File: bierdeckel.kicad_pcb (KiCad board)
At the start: 2 copper layers, 93 x 93 mm, 67 parts, among them IC1 HSFPAR004A, J1 Pogo, J2 Pogo, J6 USB4110-GF-A, Q1 BSS138P,215, SW1 PTS526 SK15 SMTR2 LFS, SW2 PTS526 SK15 SMTR2 LFS, SW3 PTS526 SK15 SMTR2 LFS, U1 ESP32-C3-WROOM-02, U2 BQ25176J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

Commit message: replace some components for JLC order
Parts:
- R21: value 4k -> 4k02
- R22: value 4k -> 5k1
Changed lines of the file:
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@@
 			)
 		)
-		(property "mpn" "CR0805-FX-1002ELF "
+		(property "mpn" ""
 			(at 0 0 315)
 			(unlocked yes)
@@
 			)
 		)
-		(property "mpn" "CRCW08054K99FKEA"
+		(property "mpn" ""
 			(at 0 0 180)
 			(unlocked yes)
@@
 			)
 		)
-		(property "mpn" "150060GS73220"
+		(property "mpn" "A-SP192DGHC-C01-4T"
 			(at 0 0 0)
 			(layer "F.Fab")
@@
 		(sheetname "/LEDs/")
 		(sheetfile "leds.kicad_sch")
-		(attr smd)
+		(attr smd exclude_from_bom dnp)
 		(fp_line
 			(start -1 1.05)
@@
 			)
 		)
+		(property "mpn" "ESP32-C3-WROOM-02"
+			(at 0 0 0)
+			(unlocked yes)
+			(layer "F.Fab")
+			(hide yes)
+			(effects
+				(font
+					(size 1 1)
+					(thickness 0.15)
+				)
+			)
+		)
 		(property ki_fp_filters "ESP32?C3*WROOM?02*")
 		(sheetname "/")
@@
 			)
 		)
-		(property "mpn" ""
+		(property "mpn" "BSS138P,215"
 			(at 0 0 180)
 			(unlocked yes)
@@
 			)
 		)
-		(property "mpn" "CRCW080562K0FKEA"
+		(property "mpn" ""
 			(at 0 0 0)
 			(unlocked yes)
@@
 		(sheetfile "bierdeckel.kicad_sch")
 		(zone_connect 1)
-		(attr exclude_from_pos_files allow_soldermask_bridges)
+		(attr exclude_from_pos_files exclude_from_bom dnp allow_soldermask_bridges)
 		(fp_rect
 			(start -0.15 -0.75)
@@
 			)
 		)
+		(property "mpn" "1N4148WT"
+			(at 0 0 0)
+			(unlocked yes)
+			(layer "F.Fab")
+			(hide yes)
+			(effects
+				(font
+					(size 1 1)
+					(thickness 0.15)
+				)
+			)
+		)
 		(property ki_fp_filters "D*SOD?523*")
 		(sheetname "/")
@@
 		(sheetfile "bierdeckel.kicad_sch")
 		(zone_connect 1)
-		(attr exclude_from_pos_files allow_soldermask_bridges)
+		(attr exclude_from_pos_files exclude_from_bom dnp allow_soldermask_bridges)
 		(fp_rect
 			(start -0.15 -0.75)
@@
 			)
 		)
-		(property "mpn" "CRCW08054K99FKEA"
+		(property "mpn" ""
 			(at 0 0 270)
 			(unlocked yes)
@@
 			)
 		)
-		(property "mpn" "CR0805-FX-1002ELF "
+		(property "mpn" ""
 			(at 0 0 90)
 			(unlocked yes)
@@
 			)
 		)
-		(property "mpn" "CRCW080562K0FKEA"
+		(property "mpn" ""
 			(at 0 0 180)
 			(unlocked yes)
@@
 			)
 		)
-		(property "mpn" "CR0805-FX-1002ELF "
+		(property "mpn" ""
 			(at 0 0 90)
 			(unlocked yes)
@@
 			)
 		)
-		(property "mpn" "CR0805-FX-1002ELF "
+		(property "mpn" ""
 			(at 0 0 90)
 			(unlocked yes)
@@
 		(sheetfile "bierdeckel.kicad_sch")
 		(zone_connect 1)
-		(attr exclude_from_pos_files allow_soldermask_bridges)
+		(attr exclude_from_pos_files exclude_from_bom dnp allow_soldermask_bridges)
 		(fp_rect
 			(start -0.15 -0.75)
@@
 			)
 		)
-		(property "mpn" "CR0805-FX-1002ELF "
+		(property "mpn" ""
 			(at 0 0 270)
 			(unlocked yes)
@@
 			)
 		)
-		(property "mpn" "CRCW08054K99FKEA"
+		(property "mpn" ""
 			(at 0 0 270)
 			(unlocked yes)
@@
 			)
 		)
+		(property "mpn" "HSFPAR004A"
+			(at 0 0 315)
+			(unlocked yes)
+			(layer "F.Fab")
+			(hide yes)
+			(effects
+				(font
+					(size 1 1)
+					(thickness 0.15)
+				)
+			)
+		)
 		(sheetname "/Pressure Gauge/")
 		(sheetfile "pressure.kicad_sch")
@@
 			)
 		)
-		(property "mpn" "CRCW080527K4FKEA"
+		(property "mpn" ""
 			(at 0 0 270)
 			(unlocked yes)
@@
 			)
 		)
-		(property "mpn" "CRCW08054K99FKEA"
+		(property "mpn" ""
 			(at 0 0 0)
 			(unlocked yes)
@@
 			)
 		)
-		(property "mpn" "CR0805-FX-6200ELF "
+		(property "mpn" ""
 			(at 0 0 90)
 			(unlocked yes)
@@
 			)
 		)
-		(property "mpn" "CRCW08054K99FKEA"
+		(property "mpn" ""
 			(at 0 0 180)
 			(unlocked yes)
@@
 			)
 		)
-		(property "mpn" "CR0805-FX-1002ELF "
+		(property "mpn" ""
 			(at 0 0 270)
 			(unlocked yes)
@@
 			)
 		)
-		(property "mpn" "CR0805-FX-1002ELF "
+		(property "mpn" ""
 			(at 0 0 180)
 			(unlocked yes)
@@
 			)
 		)
-		(property "mpn" "CR0805-FX-1002ELF "
+		(property "mpn" ""
 			(at 0 0 270)
 			(unlocked yes)
@@
 			)
 		)
-		(property "Value" "4k"
+		(property "Value" "4k02"
 			(at 0 1.83 90)
 			(layer "F.Fab")
@@
 			)
 		)
-		(property "mpn" "CR0805-FX-1002ELF "
+		(property "mpn" "RC1206FR-074K02L"
 			(at 0 0 90)
 			(unlocked yes)
@@
 			)
 		)
-		(property "mpn" "150060BS73220"
+		(property "mpn" "XL-1608UBC-04"
 			(at 0 0 0)
 			(layer "F.Fab")
@@
 			)
 		)
+		(property "mpn" "INA317IDGKR"
+			(at 0 0 270)
+			(unlocked yes)
+			(layer "F.Fab")
+			(hide yes)
+			(effects
+				(font
+					(size 1 1)
+					(thickness 0.15)
+				)
+			)
+		)
 		(sheetname "/Pressure Gauge/")
 		(sheetfile "pressure.kicad_sch")
@@
 			)
 		)
-		(property "mpn" "CL21A106KPFNNNF"
+		(property "mpn" "CL21B105KAFNNNG "
 			(at 0 0 0)
 			(unlocked yes)
@@
 			)
 		)
-		(property "Value" "4k"
+		(property "Value" "5k1"
 			(at 0 1.43 0)
 			(layer "F.Fab")
@@
 			)
 		)
-		(property "mpn" "CR0805-FX-1002ELF "
+		(property "mpn" ""
 			(at 0 0 180)
 			(unlocked yes)

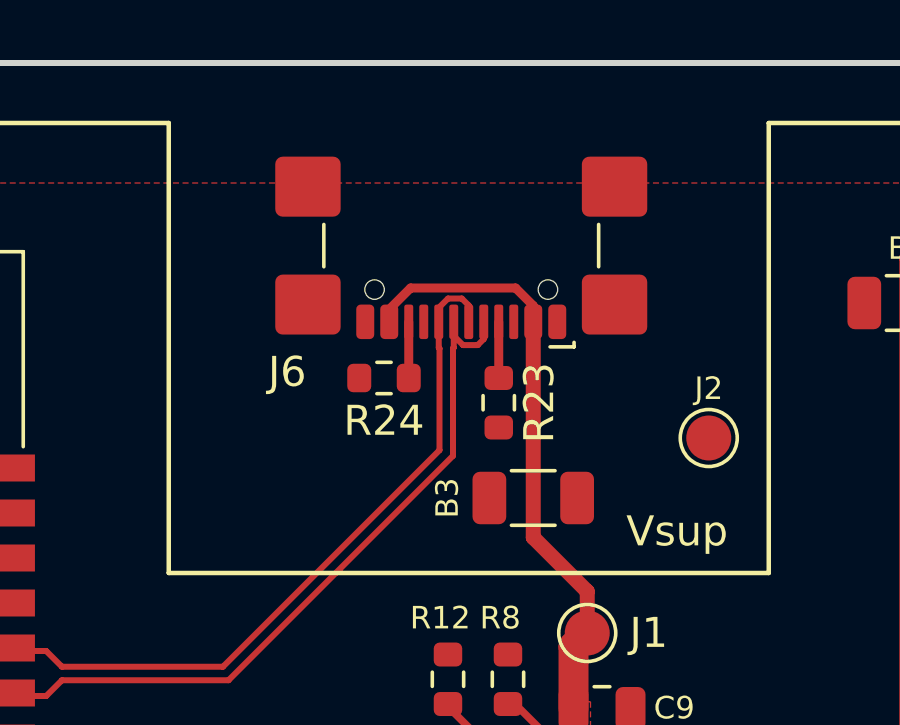
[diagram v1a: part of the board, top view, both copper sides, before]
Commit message: update PCB usb position and further base work
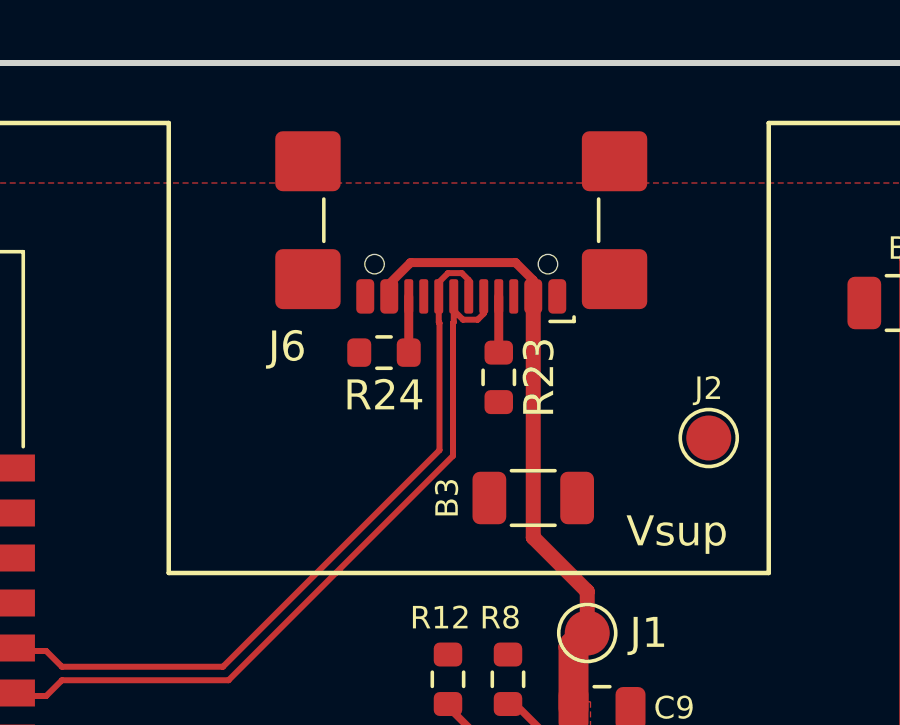
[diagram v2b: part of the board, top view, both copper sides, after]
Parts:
- moved J6 0.85 mm to (162.2, 54.1)
- moved R23 0.85 mm to (163.5, 60.5)
- moved R24 0.85 mm to (159.7, 59.7)
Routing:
- net /USB-: track 24.7 -> 25.6 mm
- net /USB+: track 24.0 -> 24.8 mm
- net /Vcharge: track 22.9 -> 23.7 mm
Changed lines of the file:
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@@
 	(footprint "Connector_USB:USB_C_Receptacle_GCT_USB4110"
 		(layer "F.Cu")
-		(at 162.25 54.947 180)
+		(at 162.25 54.1 180)
 		(descr "USB 2.0 Type C Receptacle, GCT, 16P, top mounted, horizontal, 5A, https://gct.co/files/drawings/usb4110.pdf")
 		(tags "USB 2.0 C Type-C Receptacle SMD 16P 16C USB4110-GF-A")
@@
 	(footprint "Resistor_SMD:R_0603_1608Metric"
 		(layer "F.Cu")
-		(at 163.5 61.325 -90)
+		(at 163.5 60.478 -90)
 		(descr "Resistor SMD 0603 (1608 Metric), square (rectangular) end terminal, IPC-7351 nominal, (Body size source: IPC-SM-782 page 72, https://www.pcb-3d.com/wordpress/wp-content/uploads/ipc-sm-782a_amendment_1_and_2.pdf), generated with kicad-footprint-generator")
 		(tags "resistor")
@@
 	(footprint "Resistor_SMD:R_0603_1608Metric"
 		(layer "F.Cu")
-		(at 159.675 60.5 180)
+		(at 159.675 59.653 180)
 		(descr "Resistor SMD 0603 (1608 Metric), square (rectangular) end terminal, IPC-7351 nominal, (Body size source: IPC-SM-782 page 72, https://www.pcb-3d.com/wordpress/wp-content/uploads/ipc-sm-782a_amendment_1_and_2.pdf), generated with kicad-footprint-generator")
 		(tags "resistor")
@@
 	)
 	(segment
-		(start 166.45 67.615001)
-		(end 164.65 65.815001)
-		(width 0.5)
-		(layer "F.Cu")
-		(net 11)
-	)
-	(segment
-		(start 164.061281 57.5)
-		(end 164.65 58.088719)
+		(start 164.061281 56.653)
+		(end 164.65 57.241719)
 		(width 0.3)
 		(layer "F.Cu")
@@
 	)
 	(segment
-		(start 159.85 58.212)
-		(end 160.562 57.5)
+		(start 159.85 57.365)
+		(end 160.562 56.653)
 		(width 0.3)
 		(layer "F.Cu")
@@
 	)
 	(segment
-		(start 165.9925 69.4575)
-		(end 166.45 69)
-		(width 1)
+		(start 164.65 65.815001)
+		(end 164.65 57.78)
+		(width 0.5)
 		(layer "F.Cu")
 		(net 11)
 	)
 	(segment
-		(start 164.65 65.815001)
-		(end 164.65 58.627)
+		(start 166.45 67.615001)
+		(end 164.65 65.815001)
 		(width 0.5)
 		(layer "F.Cu")
@@
 	)
 	(segment
-		(start 166.45 69)
-		(end 166.45 67.615001)
-		(width 0.5)
+		(start 165.9925 69.4575)
+		(end 166.45 69)
+		(width 1)
 		(layer "F.Cu")
 		(net 11)
@@
 	)
 	(segment
-		(start 159.85 58.627)
-		(end 159.85 58.212)
+		(start 159.85 57.78)
+		(end 159.85 57.365)
 		(width 0.3)
 		(layer "F.Cu")
@@
 	)
 	(segment
-		(start 164.65 58.088719)
-		(end 164.65 58.627)
+		(start 164.65 57.241719)
+		(end 164.65 57.78)
 		(width 0.3)
 		(layer "F.Cu")
@@
 	)
 	(segment
-		(start 160.562 57.5)
-		(end 164.061281 57.5)
+		(start 160.562 56.653)
+		(end 164.061281 56.653)
 		(width 0.3)
 		(layer "F.Cu")
@@
 	)
 	(segment
+		(start 166.45 69)
+		(end 166.45 67.615001)
+		(width 0.5)
+		(layer "F.Cu")
+		(net 11)
+	)
+	(segment
 		(start 143.251 78.539448)
 		(end 143.251 69.524)
@@
 	)
 	(segment
-		(start 162 59.489501)
-		(end 161.975 59.514501)
+		(start 161.975 63.093198)
+		(end 154.493198 70.575)
 		(width 0.2)
 		(layer "F.Cu")
@@
 	)
 	(segment
-		(start 161.975 63.093198)
-		(end 154.493198 70.575)
+		(start 148.940001 70.575)
+		(end 148.415001 71.1)
 		(width 0.2)
 		(layer "F.Cu")
@@
 	)
 	(segment
-		(start 162 58.627)
-		(end 162 59.094402)
+		(start 162 57.78)
+		(end 162 58.247402)
 		(width 0.2)
 		(layer "F.Cu")
@@
 	)
 	(segment
-		(start 161.975 59.514501)
-		(end 161.975 63.093198)
+		(start 154.493198 70.575)
+		(end 148.940001 70.575)
 		(width 0.2)
 		(layer "F.Cu")
@@
 	)
 	(segment
-		(start 162 59.094402)
-		(end 162.308598 59.403)
+		(start 162 57.78)
+		(end 162 58.642501)
 		(width 0.2)
 		(layer "F.Cu")
@@
 	)
 	(segment
-		(start 154.493198 70.575)
-		(end 148.940001 70.575)
+		(start 162 58.247402)
+		(end 162.308598 58.556)
 		(width 0.2)
 		(layer "F.Cu")
@@
 	)
 	(segment
-		(start 162.308598 59.403)
-		(end 162.798999 59.403)
+		(start 162 58.642501)
+		(end 161.975 58.667501)
 		(width 0.2)
 		(layer "F.Cu")
@@
 	)
 	(segment
-		(start 163 59.201999)
-		(end 163 58.627)
+		(start 161.975 58.667501)
+		(end 161.975 63.093198)
 		(width 0.2)
 		(layer "F.Cu")
@@
 	)
 	(segment
-		(start 162.798999 59.403)
-		(end 163 59.201999)
+		(start 162.308598 58.556)
+		(end 162.798999 58.556)
 		(width 0.2)
 		(layer "F.Cu")
@@
 	)
 	(segment
-		(start 148.940001 70.575)
-		(end 148.415001 71.1)
+		(start 163 58.354999)
+		(end 163 57.78)
 		(width 0.2)
 		(layer "F.Cu")
@@
 	)
 	(segment
-		(start 162 58.627)
-		(end 162 59.489501)
+		(start 162.798999 58.556)
+		(end 163 58.354999)
 		(width 0.2)
 		(layer "F.Cu")
@@
 	)
 	(segment
-		(start 161.808598 57.851)
-		(end 162.269 57.851)
+		(start 148.415001 69.6)
+		(end 147.29 69.6)
 		(width 0.2)
 		(layer "F.Cu")
@@
 	)
 	(segment
-		(start 148.940001 70.125)
-		(end 148.415001 69.6)
+		(start 161.5 57.78)
+		(end 161.5 58.642501)
 		(width 0.2)
 		(layer "F.Cu")
@@
 	)
 	(segment
-		(start 154.306802 70.125)
-		(end 148.940001 70.125)
+		(start 161.525 58.667501)
+		(end 161.525 62.906802)
 		(width 0.2)
 		(layer "F.Cu")
@@
 	)
 	(segment
-		(start 161.5 58.627)
-		(end 161.5 59.489501)
+		(start 161.808598 57.004)
+		(end 162.269 57.004)
 		(width 0.2)
 		(layer "F.Cu")
@@
 	)
 	(segment
-		(start 162.269 57.851)
-		(end 162.5 58.082)
+		(start 148.940001 70.125)
+		(end 148.415001 69.6)
 		(width 0.2)
 		(layer "F.Cu")
@@
 	)
 	(segment
-		(start 161.5 58.159598)
-		(end 161.808598 57.851)
+		(start 154.306802 70.125)
+		(end 148.940001 70.125)
 		(width 0.2)
 		(layer "F.Cu")
@@
 	)
 	(segment
-		(start 161.525 62.906802)
-		(end 154.306802 70.125)
+		(start 161.5 58.642501)
+		(end 161.525 58.667501)
 		(width 0.2)
 		(layer "F.Cu")
@@
 	)
 	(segment
-		(start 161.525 59.514501)
-		(end 161.525 62.906802)
+		(start 162.269 57.004)
+		(end 162.5 57.235)
 		(width 0.2)
 		(layer "F.Cu")
@@
 	)
 	(segment
-		(start 161.5 58.627)
-		(end 161.5 58.159598)
+		(start 161.5 57.312598)
+		(end 161.808598 57.004)
 		(width 0.2)
 		(layer "F.Cu")
@@
 	)
 	(segment
-		(start 148.415001 69.6)
-		(end 147.29 69.6)
+		(start 161.525 62.906802)
+		(end 154.306802 70.125)
 		(width 0.2)
 		(layer "F.Cu")
@@
 	)
 	(segment
-		(start 161.5 59.489501)
-		(end 161.525 59.514501)
+		(start 161.5 57.78)
+		(end 161.5 57.312598)
 		(width 0.2)
 		(layer "F.Cu")
@@
 	)
 	(segment
-		(start 162.5 58.082)
-		(end 162.5 58.627)
+		(start 162.5 57.235)
+		(end 162.5 57.78)
 		(width 0.2)
 		(layer "F.Cu")
@@
 	)
 	(segment
-		(start 163.5 58.627)
-		(end 163.5 60.5)
+		(start 163.5 57.78)
+		(end 163.5 59.653)
 		(width 0.3)
 		(layer "F.Cu")
@@
 	)
 	(segment
-		(start 160.5 58.627)
-		(end 160.5 60.5)
+		(start 160.5 57.78)
+		(end 160.5 59.653)
 		(width 0.3)
 		(layer "F.Cu")
@@
 	(group ""
 		(members "029e82b0-6f87-4dab-a816-896787e5f8be" "060ef96b-ab42-421e-bec1-6ab20f4b8b19"
-			"1b3538c2-d924-4c36-869f-3fc17f00636d" "1c10c983-b24e-473c-a313-67251e28e691"
-			"22be54e4-b058-4085-8689-9657ceccbf3d" "264485a5-6322-4f09-a541-025527a220d0"
-			"291e3ef5-2d30-4bb5-b147-5e44f73acd7d" "3190285a-c7d1-4f60-ad83-9c7b89209e60"
+			"1c10c983-b24e-473c-a313-67251e28e691" "22be54e4-b058-4085-8689-9657ceccbf3d"
+			"264485a5-6322-4f09-a541-025527a220d0" "291e3ef5-2d30-4bb5-b147-5e44f73acd7d"
+			"311c0f60-6760-4d45-8ee4-6125138ab151" "3190285a-c7d1-4f60-ad83-9c7b89209e60"
 			"3486287d-a9ab-4a03-9302-ff86736020e4" "34f8ebb7-c6ad-4c2b-9aae-d918b22fa308"
 			"37faf9e4-efa1-4549-9664-62bf4775f514" "3b493488-0e8e-46e8-964e-859a8e7eac88"
 			"434d4e8b-8ed2-48e0-a07d-b9c6d2e028de" "43c951d3-8a55-45ce-92bb-3d6a5361e630"
 			"4888f7f7-d75b-4f0b-bfa3-71ab310586f3" "4cc79c58-c1ea-4931-895d-0a8789d40b33"
-			"6107b0e4-5ddd-4981-8d1f-1183a42032d2" "624eb6cd-d45c-4e05-aa4a-72f4b4ba11ab"
-			"6b7f1c43-536b-4622-97b4-c4f44ccc9bf8" "6db57d69-e72a-422c-8234-ed3925f108b9"
-			"73a65b63-1af1-4f85-89d8-619294574655" "765884f0-f1f7-4810-812e-bc8a56450143"
-			"7973b36f-f058-44c8-abf5-a3ff40129970" "8219f3c5-fe80-417e-af57-5687dd099cc7"
-			"84043802-128f-45e6-b08e-d7778fa1858c" "8be5026b-cac2-4d1a-9b88-d7e6ff8bfb28"
-			"95be49f8-da1a-4a99-8b36-b1ad6315d803" "9cd0eab5-4517-4ede-8155-68cf644196bd"
-			"a36d3142-b6c0-4f46-a08e-0c92065e6637" "ae028d0f-a6cc-4d4d-8ec7-b25c6611ac60"
-			"ba83582b-ce96-4a23-8e12-c83c717a308f" "c04243c4-3eb5-4115-8e3e-d0b1f092c72f"
-			"c6e85f69-5874-4954-971d-0c9ba822e001" "c77631c4-de12-4287-a936-32a4eab5b0c8"
-			"cbc9eb7d-e4a3-4e86-af29-53c97b6e2414" "d18f15b0-6d6b-44b0-a3b6-b828a7268238"
-			"d23b3f9b-c099-46f8-bbe7-23aa6451095e" "d24525c7-14a0-4847-b370-d8e90ac9d301"
-			"d39cccff-d7ee-4fef-9fc7-bc620502d21d" "d78a606b-8c03-4298-bdb9-a5644453ccec"
-			"d9062dfe-38f0-4de2-9271-38ce9c8d8ffe" "ddee5308-8cc2-4952-9ce7-1be5d412332b"
+			"50f4aeff-45d8-449a-9674-1e836492e021" "6107b0e4-5ddd-4981-8d1f-1183a42032d2"
+			"624eb6cd-d45c-4e05-aa4a-72f4b4ba11ab" "6b7f1c43-536b-4622-97b4-c4f44ccc9bf8"
+			"6db57d69-e72a-422c-8234-ed3925f108b9" "73a65b63-1af1-4f85-89d8-619294574655"
+			"765884f0-f1f7-4810-812e-bc8a56450143" "7973b36f-f058-44c8-abf5-a3ff40129970"
+			"8be5026b-cac2-4d1a-9b88-d7e6ff8bfb28" "95be49f8-da1a-4a99-8b36-b1ad6315d803"
+			"9cd0eab5-4517-4ede-8155-68cf644196bd" "a36d3142-b6c0-4f46-a08e-0c92065e6637"
+			"ae028d0f-a6cc-4d4d-8ec7-b25c6611ac60" "ba83582b-ce96-4a23-8e12-c83c717a308f"
+			"c04243c4-3eb5-4115-8e3e-d0b1f092c72f" "c6e85f69-5874-4954-971d-0c9ba822e001"
+			"c77631c4-de12-4287-a936-32a4eab5b0c8" "cbc9eb7d-e4a3-4e86-af29-53c97b6e2414"
+			"d18f15b0-6d6b-44b0-a3b6-b828a7268238" "d23b3f9b-c099-46f8-bbe7-23aa6451095e"
+			"d24525c7-14a0-4847-b370-d8e90ac9d301" "d39cccff-d7ee-4fef-9fc7-bc620502d21d"
+			"d78a606b-8c03-4298-bdb9-a5644453ccec" "d9062dfe-38f0-4de2-9271-38ce9c8d8ffe"
+			"dc6e5dfd-728c-45b8-a6d7-8bcd14c3b581" "ddee5308-8cc2-4952-9ce7-1be5d412332b"
 			"df9951c1-17b9-4dca-9e1b-88526affb058" "e0e5c99a-9d5e-4c2a-aaf5-ee9fd11e5c2b"
 			"e1575d1d-4c74-44cc-965e-b3397effc8b5" "ecf4a1a5-47ad-4070-9a33-ef9ba32593cd"
